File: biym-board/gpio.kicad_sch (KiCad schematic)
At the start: 1 part, among them J6 HEADER_01X03_JST_ZH_SMD_VERTI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

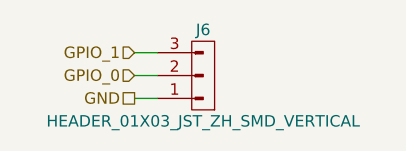
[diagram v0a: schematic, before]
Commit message: Move gpio pins to rx and tx pins
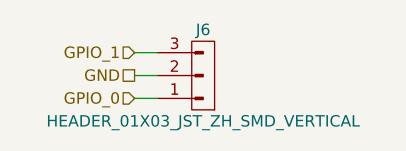
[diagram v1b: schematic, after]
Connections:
- net GND: now also J6.2 (Pin_2); no longer J6.1 (Pin_1)
- net GPIO_0: now also J6.1 (Pin_1); no longer J6.2 (Pin_2)
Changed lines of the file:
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@@
     (company "Peter Polidoro")
   )
-  (wire (pts (xy 134.62 96.52) (xy 137.16 96.52))
+  (wire (pts (xy 134.62 93.98) (xy 137.16 93.98))
     (stroke (width 0) (type default) (color 0 0 0 0))
   )
-  (wire (pts (xy 134.62 93.98) (xy 137.16 93.98))
+  (wire (pts (xy 134.62 96.52) (xy 137.16 96.52))
     (stroke (width 0) (type default) (color 0 0 0 0))
   )
@@
     (stroke (width 0) (type default) (color 0 0 0 0))
   )
-  (hierarchical_label "GPIO_0" (shape input) (at 134.62 93.98 180)
+  (hierarchical_label "GPIO_0" (shape input) (at 134.62 96.52 180)
     (effects (font (size 1.27 1.27)) (justify right))
   )
-  (hierarchical_label "GND" (shape passive) (at 134.62 96.52 180)
+  (hierarchical_label "GND" (shape passive) (at 134.62 93.98 180)
     (effects (font (size 1.27 1.27)) (justify right))
   )

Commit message: Update to kicad 7
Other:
- title: biym-board-gpio -> biym-board
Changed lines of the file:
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@@
-(kicad_sch (version 20211123) (generator eeschema)
+(kicad_sch (version 20230121) (generator eeschema)
   (paper "A4")
   (title_block
-    (title "biym-board-gpio")
-    (date "2022-11-29")
+    (title "biym-board")
+    (date "2024-05-16")
     (rev "1.3")
     (company "Peter Polidoro")
   )
   (wire (pts (xy 134.62 93.98) (xy 137.16 93.98))
-    (stroke (width 0) (type default) (color 0 0 0 0))
+    (stroke (width 0) (type default))
   )
   (wire (pts (xy 134.62 96.52) (xy 137.16 96.52))
-    (stroke (width 0) (type default) (color 0 0 0 0))
+    (stroke (width 0) (type default))
   )
   (wire (pts (xy 134.62 91.44) (xy 137.16 91.44))
-    (stroke (width 0) (type default) (color 0 0 0 0))
+    (stroke (width 0) (type default))
   )
-  (hierarchical_label "GPIO_0" (shape input) (at 134.62 96.52 180)
+  (hierarchical_label "GPIO_0" (shape input) (at 134.62 96.52 180) (fields_autoplaced)
     (effects (font (size 1.27 1.27)) (justify right))
   )
-  (hierarchical_label "GND" (shape passive) (at 134.62 93.98 180)
+  (hierarchical_label "GND" (shape passive) (at 134.62 93.98 180) (fields_autoplaced)
     (effects (font (size 1.27 1.27)) (justify right))
   )
-  (hierarchical_label "GPIO_1" (shape input) (at 134.62 91.44 180)
+  (hierarchical_label "GPIO_1" (shape input) (at 134.62 91.44 180) (fields_autoplaced)
     (effects (font (size 1.27 1.27)) (justify right))
   )
   (symbol (lib_id "Janelia:HEADER_01X03_JST_ZH_SMD_VERTICAL") (at 142.24 93.98 180) (unit 1)
-    (in_bom yes) (on_board yes)
-    (property "Reference" "J6" (id 0) (at 142.24 88.9 0))
-    (property "Value" "HEADER_01X03_JST_ZH_SMD_VERTICAL" (id 1) (at 142.24 99.06 0))
-    (property "Footprint" "Janelia:JST_ZH_B3B_ZR_SM4_TF_1x03-1MP_P1.50mm_Vertical" (id 2) (at 142.24 106.68 0)
+    (in_bom yes) (on_board yes) (dnp no)
+    (property "Reference" "J6" (at 142.24 88.9 0)
+      (effects (font (size 1.27 1.27)))
+    )
+    (property "Value" "HEADER_01X03_JST_ZH_SMD_VERTICAL" (at 142.24 99.06 0)
+      (effects (font (size 1.27 1.27)))
+    )
+    (property "Footprint" "Janelia:JST_ZH_B3B_ZR_SM4_TF_1x03-1MP_P1.50mm_Vertical" (at 142.24 106.68 0)
       (effects (font (size 1.27 1.27)) hide)
     )
-    (property "Datasheet" "" (id 3) (at 142.24 93.98 0)
+    (property "Datasheet" "" (at 142.24 93.98 0)
       (effects (font (size 1.27 1.27)) hide)
     )
-    (property "Description" "CONN HEADER SMD 3POS 1.5MM" (id 4) (at 142.24 104.14 0)
+    (property "Description" "CONN HEADER SMD 3POS 1.5MM" (at 142.24 104.14 0)
       (effects (font (size 1.27 1.27)) hide)
     )
-    (property "Manufacturer" "JST Sales America Inc." (id 5) (at 142.24 111.76 0)
+    (property "Manufacturer" "JST Sales America Inc." (at 142.24 111.76 0)
       (effects (font (size 1.27 1.27)) hide)
     )
-    (property "Manufacturer Part Number" "B3B-ZR-SM4-TF(LF)(SN)" (id 6) (at 142.24 109.22 0)
+    (property "Manufacturer Part Number" "B3B-ZR-SM4-TF(LF)(SN)" (at 142.24 109.22 0)
       (effects (font (size 1.27 1.27)) hide)
     )
-    (property "Vendor" "Digi-Key" (id 7) (at 142.24 114.3 0)
+    (property "Vendor" "Digi-Key" (at 142.24 114.3 0)
       (effects (font (size 1.27 1.27)) hide)
     )
-    (property "Vendor Part Number" "B3B-ZR-SM4-TF(LF)(SN)" (id 8) (at 142.24 116.84 0)
+    (property "Vendor Part Number" "B3B-ZR-SM4-TF(LF)(SN)" (at 142.24 116.84 0)
       (effects (font (size 1.27 1.27)) hide)
     )
@@
     (pin "2")
     (pin "3")
+    (instances
+      (project "biym-board"
+        (path "/8aa5116f-ac54-4325-a42a-36123c2901d1/5a587278-0eec-4b8f-b1d6-43d5ddf30d13"
+          (reference "J6") (unit 1)
+        )
+      )
+    )
   )
 )
